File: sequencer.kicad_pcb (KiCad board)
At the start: 2 copper layers, 171.4 x 106.7 mm, 435 parts, among them J1 PJ301CM, J10 PJ301BM, J11 PJ301BM, J12 PJ301BM, J13 PJ301BM, J14 PJ301BM, J15 PJ301BM, J16 PJ301BM, J17 PJ301BM, J18 PJ301BM, J19 PJ301BM, J2 PJ301CM, J20 PJ301BM, J21 PJ301BM, J22 PJ301BM, J23 PJ301BM, J24 PJ301BM, J25 PJ301BM, J26 PJ301BM, J3 PJ301BM, J4 PJ301BM, J5 PJ301BM, J6 PJ301BM, J7 PJ301BM, J8 PJ301BM, J9 PJ301BM, Q1 MMBT3904, Q2 MMBT3904, Q3 MMBT3904, Q4 MMBT3904, Q5 MMBT3904, SW1 TL1105, SW10 TL1105, SW11 TL1105, SW12 TL1105, SW13 TL1105, SW14 TL1105, SW15 TL1105, SW16 TL1105, SW17 TL1105, SW18 TL1105, SW19 EVQQ2, SW2 TL1105, SW20 TL1105, SW21 TL1105, SW22 TL1105, SW23 TL1105, SW24 TL1105, SW25 TL1105, SW26 TL1105, SW27 TL1105, SW28 TL1105, SW29 TL1105, SW3 TL1105, SW30 TL1105, SW31 TL1105, SW32 TL1105, SW33 TL1105, SW34 TL1105, SW35 TL1105, SW36 TL1105, SW37 TL1105, SW38 TL1105, SW39 TL1105, SW4 TL1105, SW5 TL1105, SW6 TL1105, SW7 TL1105, SW8 EVQQ2, SW9 TL1105, U1 VO0600T, U10 LM1117-3.3, U11 74HC165, U12 74HC595, U13 74HC595, U14 74HC595, U15 OPA4172, U16 R-78E5.0-1.0, U2 74LV1T34, U3 STMPS2151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

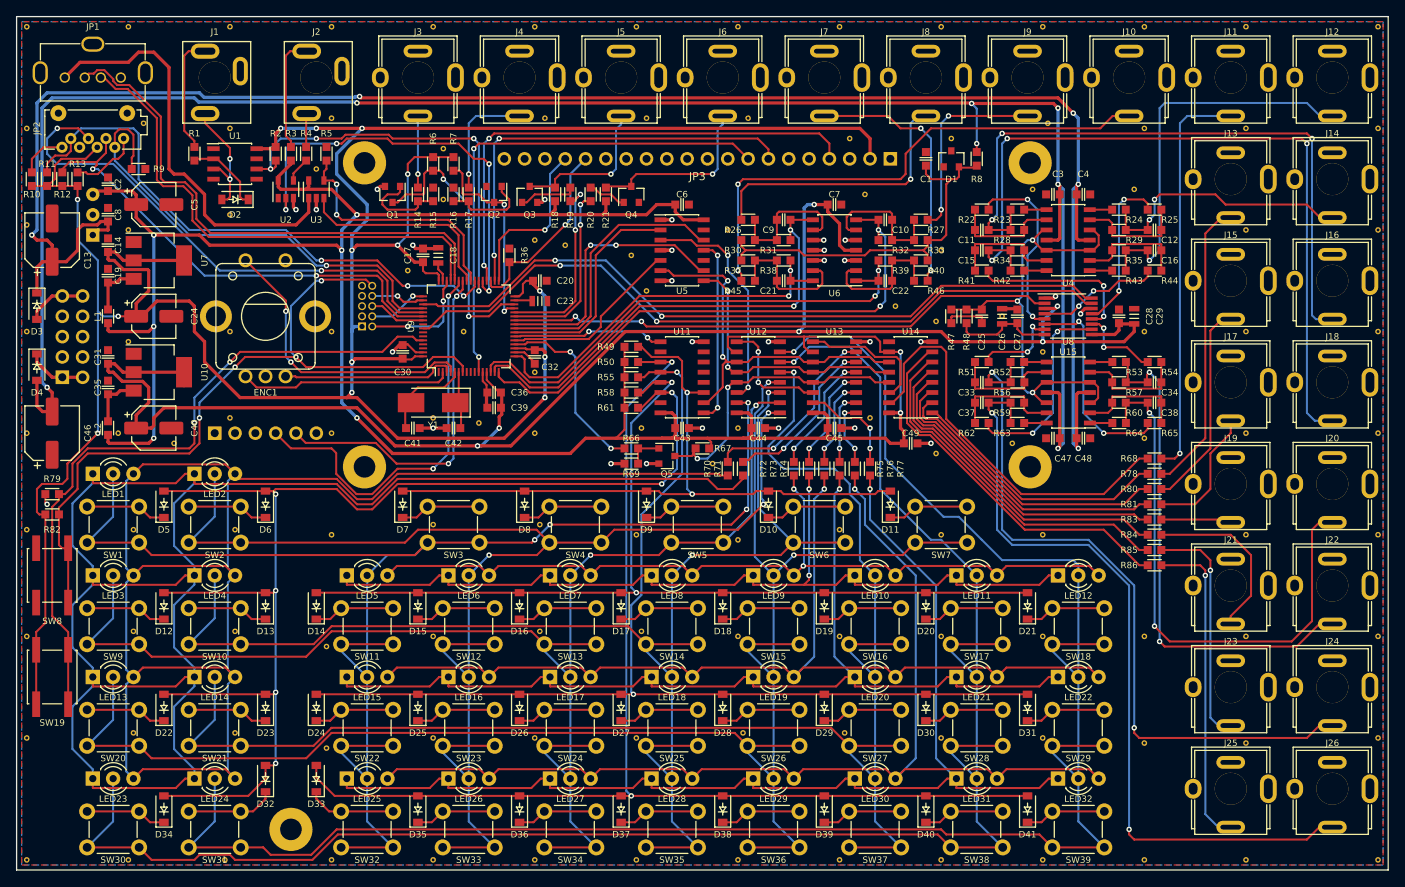
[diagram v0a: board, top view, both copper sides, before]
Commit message: replaced jacks with thonkiconns, updated pcb routing
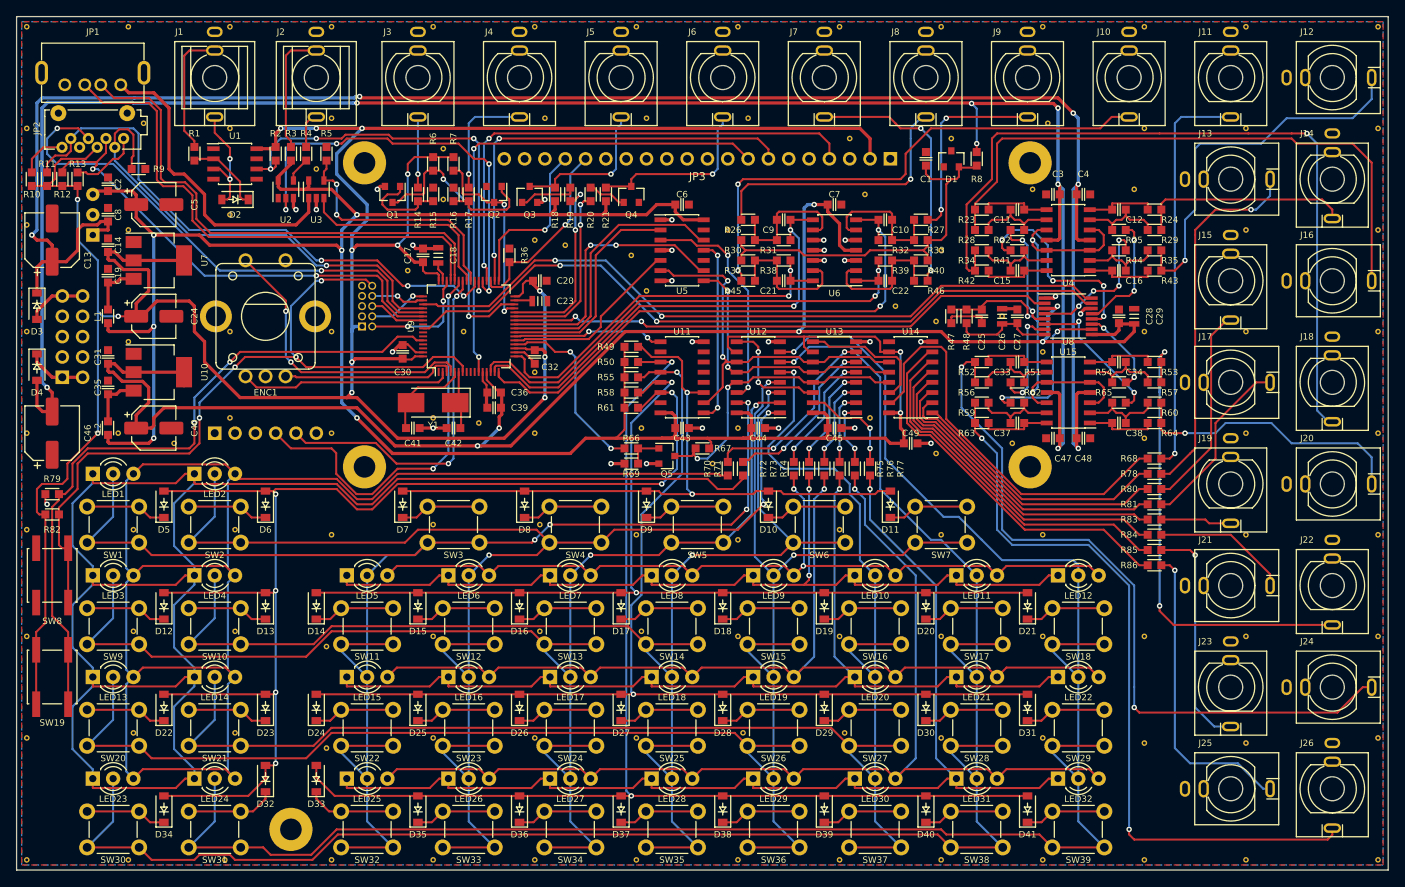
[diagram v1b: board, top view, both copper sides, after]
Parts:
- J1, J2: footprint w_connector:PJ301CM_OFFSET -> w_connector:PJ366ST_Compact
- J10, J11, J12, J13, J14, J15, J16, J17, J18, J19, J20, J21, J22, J23, J24, J25, J26, J3, J4, J5, J6, J7, J8, J9: value PJ301BM -> PJ301M-12_Compact; footprint w_connector:PJ301BM -> w_connector:PJ301M-12_Compact
- JP1: footprint w_connector:MOLEX_USB_105057 -> w_connector:Kycon_USB_KUSBVLPX-AS1N
- moved C37 5.12 mm to (201.9, 88.9)
- moved C38 5.12 mm to (214.6, 88.9)
- moved R62 5.12 mm to (201.9, 86.4), turned to 180 degrees
- moved R65 5.12 mm to (214.6, 86.4), turned to 0 degrees
- moved C11 5.12 mm to (201.9, 62.2)
- moved C12 5.12 mm to (214.6, 62.2)
- moved R22 5.12 mm to (201.9, 64.8), turned to 180 degrees
- moved R25 5.12 mm to (214.6, 64.8), turned to 0 degrees
- moved C15 5.12 mm to (201.9, 69.8)
- moved C16 5.12 mm to (214.6, 69.8)
- moved C33 5.12 mm to (201.9, 81.3)
- moved C34 5.12 mm to (214.6, 81.3)
- moved R41 5.12 mm to (201.9, 67.3), turned to 180 degrees
- moved R44 5.12 mm to (214.6, 67.3), turned to 0 degrees
- moved R51 5.12 mm to (201.9, 83.8), turned to 180 degrees
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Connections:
- C11 pad 1: CV3 -> Net-(C11-Pad1)
- C12 pad 1: CV2 -> Net-(C12-Pad1)
- C15 pad 1: CV4 -> Net-(C15-Pad1)
- C16 pad 1: CV1 -> Net-(C16-Pad1)
- C33 pad 1: CV7 -> Net-(C33-Pad1)
- C34 pad 1: CV6 -> Net-(C34-Pad1)
- C37 pad 1: CV8 -> Net-(C37-Pad1)
- C38 pad 1: CV5 -> Net-(C38-Pad1)
- R23 pad 2: Net-(R23-Pad2) -> Net-(C11-Pad1)
- R24 pad 2: Net-(R24-Pad2) -> Net-(C12-Pad1)
- R42 pad 2: Net-(R42-Pad2) -> Net-(C15-Pad1)
- R43 pad 2: Net-(R43-Pad2) -> Net-(C16-Pad1)
- R52 pad 2: Net-(R52-Pad2) -> Net-(C33-Pad1)
- R53 pad 2: Net-(R53-Pad2) -> Net-(C34-Pad1)
- R63 pad 2: Net-(R63-Pad2) -> Net-(C37-Pad1)
- R64 pad 2: Net-(R64-Pad2) -> Net-(C38-Pad1)
- U15 pad 1: Net-(R64-Pad2) -> Net-(C38-Pad1)
- U15 pad 14: Net-(R63-Pad2) -> Net-(C37-Pad1)
- U15 pad 7: Net-(R53-Pad2) -> Net-(C34-Pad1)
- U15 pad 8: Net-(R52-Pad2) -> Net-(C33-Pad1)
- U4 pad 1: Net-(R43-Pad2) -> Net-(C16-Pad1)
- U4 pad 14: Net-(R42-Pad2) -> Net-(C15-Pad1)
- U4 pad 7: Net-(R24-Pad2) -> Net-(C12-Pad1)
- U4 pad 8: Net-(R23-Pad2) -> Net-(C11-Pad1)
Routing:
- net CV5: track 70.5 -> 35.5 mm, vias 2 -> 1
- net USB_5V: track 52.1 -> 39.1 mm
- net DAC3: track 23.4 -> 14.3 mm
- net CV3: track 83.9 -> 75.0 mm, vias 3 -> 0
- net Net-(C33-Pad1): track 0.00 -> 8.79 mm
- net Net-(C37-Pad1): track 0.00 -> 8.79 mm
- net Net-(C16-Pad1): track 0.00 -> 8.77 mm
- net Net-(C15-Pad1): track 0.00 -> 8.77 mm
- net Net-(C12-Pad1): track 0.00 -> 8.77 mm
- net Net-(C11-Pad1): track 0.00 -> 8.77 mm
- net Net-(C34-Pad1): track 0.00 -> 8.75 mm
- net Net-(C38-Pad1): track 0.00 -> 8.75 mm
- net Net-(J13-Pad3): track 37.6 -> 46.1 mm, vias 0 -> 1
- net DAC5: track 26.2 -> 18.3 mm
- net CV2: track 33.1 -> 26.5 mm, vias 2 -> 0
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
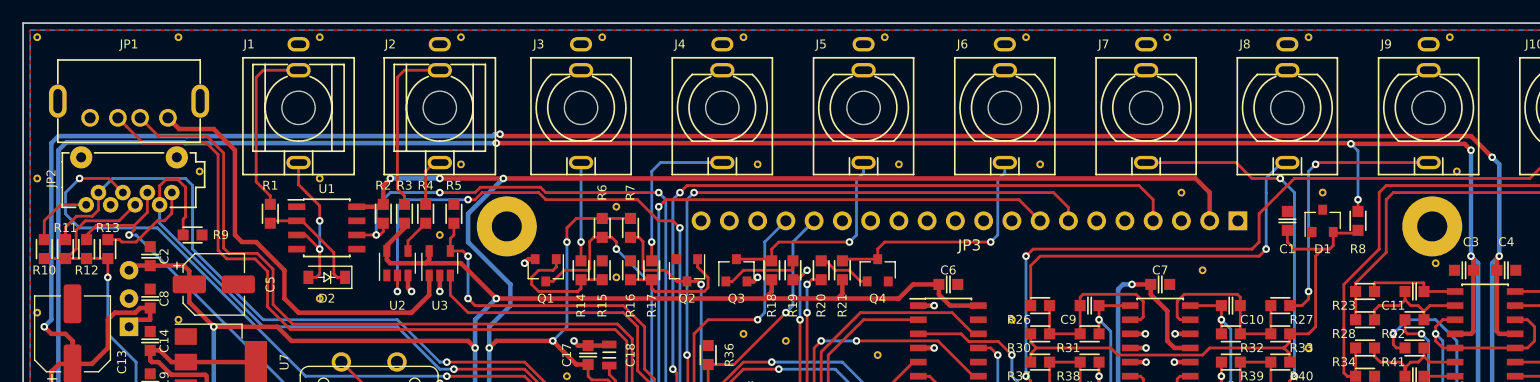
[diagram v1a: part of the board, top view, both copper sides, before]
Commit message: moved usb connector up
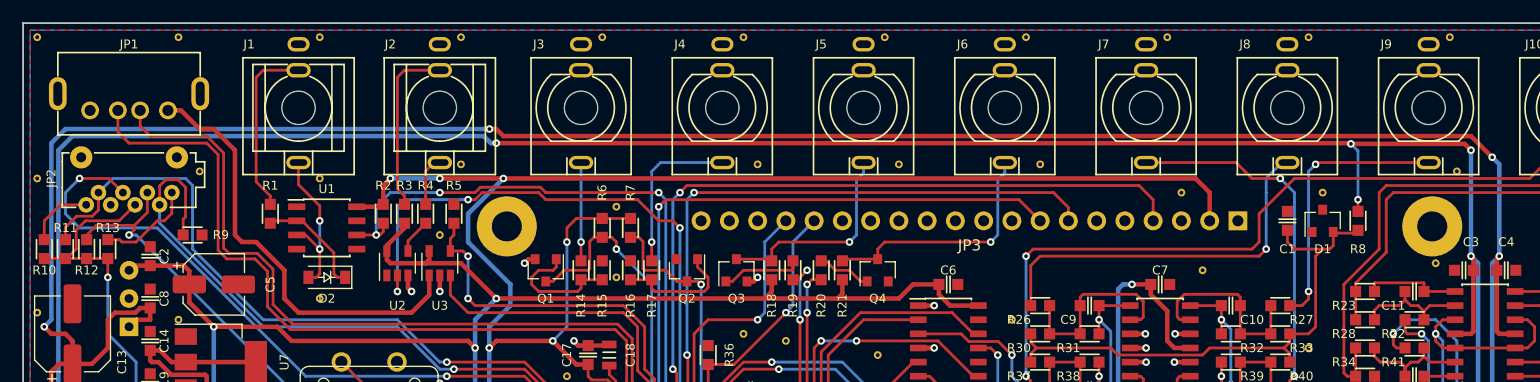
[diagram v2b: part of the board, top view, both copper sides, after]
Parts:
- moved JP1 0.67 mm to (86.4, 44.5)
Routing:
- net USB_D+: track 65.4 -> 66.8 mm
- net USB_D-: track 64.0 -> 65.1 mm

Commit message: updated component values and revision
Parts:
- J1, J2: value PJ301CM -> PJ366ST
- J10, J11, J12, J13, J14, J15, J16, J17, J18, J19, J20, J21, J22, J23, J24, J25, J26, J3, J4, J5, J6, J7, J8, J9: value PJ301M-12_Compact -> PJ398SM
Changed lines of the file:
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@@
   )
   (setup
-    (last_trace_width 0.4064)
+    (last_trace_width 0.254)
     (user_trace_width 0.254)
     (user_trace_width 0.4064)
@@
       (effects (font (size 0.8 0.8) (thickness 0.15)))
     )
-    (fp_text value PJ301M-12_Compact (at 0 0 180) (layer F.Fab)
+    (fp_text value PJ398SM (at 0 0 180) (layer F.Fab)
       (effects (font (size 1 1) (thickness 0.15)))
     )
@@
       (effects (font (size 0.8 0.8) (thickness 0.15)))
     )
-    (fp_text value PJ301M-12_Compact (at 0 0 180) (layer F.Fab)
+    (fp_text value PJ398SM (at 0 0 180) (layer F.Fab)
       (effects (font (size 1 1) (thickness 0.15)))
     )
@@
       (effects (font (size 0.8 0.8) (thickness 0.15)))
     )
-    (fp_text value PJ301M-12_Compact (at 0 0 180) (layer F.Fab)
+    (fp_text value PJ398SM (at 0 0 180) (layer F.Fab)
       (effects (font (size 1 1) (thickness 0.15)))
     )
@@
       (effects (font (size 0.8 0.8) (thickness 0.15)))
     )
-    (fp_text value PJ301M-12_Compact (at 0 0 270) (layer F.Fab)
+    (fp_text value PJ398SM (at 0 0 270) (layer F.Fab)
       (effects (font (size 1 1) (thickness 0.15)))
     )
@@
       (effects (font (size 0.8 0.8) (thickness 0.15)))
     )
-    (fp_text value PJ301M-12_Compact (at 0 0 180) (layer F.Fab)
+    (fp_text value PJ398SM (at 0 0 180) (layer F.Fab)
       (effects (font (size 1 1) (thickness 0.15)))
     )
@@
       (effects (font (size 0.8 0.8) (thickness 0.15)))
     )
-    (fp_text value PJ301M-12_Compact (at 0 0 270) (layer F.Fab)
+    (fp_text value PJ398SM (at 0 0 270) (layer F.Fab)
       (effects (font (size 1 1) (thickness 0.15)))
     )
@@
       (effects (font (size 0.8 0.8) (thickness 0.15)))
     )
-    (fp_text value PJ301M-12_Compact (at 0 0 180) (layer F.Fab)
+    (fp_text value PJ398SM (at 0 0 180) (layer F.Fab)
       (effects (font (size 1 1) (thickness 0.15)))
     )
@@
       (effects (font (size 0.8 0.8) (thickness 0.15)))
     )
-    (fp_text value PJ301M-12_Compact (at 0 0 270) (layer F.Fab)
+    (fp_text value PJ398SM (at 0 0 270) (layer F.Fab)
       (effects (font (size 1 1) (thickness 0.15)))
     )
@@
       (effects (font (size 0.8 0.8) (thickness 0.15)))
     )
-    (fp_text value PJ301M-12_Compact (at 0 0 180) (layer F.Fab)
+    (fp_text value PJ398SM (at 0 0 180) (layer F.Fab)
       (effects (font (size 1 1) (thickness 0.15)))
     )
@@
       (effects (font (size 0.8 0.8) (thickness 0.15)))
     )
-    (fp_text value PJ301M-12_Compact (at 0 0 270) (layer F.Fab)
+    (fp_text value PJ398SM (at 0 0 270) (layer F.Fab)
       (effects (font (size 1 1) (thickness 0.15)))
     )
@@
       (effects (font (size 0.8 0.8) (thickness 0.15)))
     )
-    (fp_text value PJ301M-12_Compact (at 0 0 180) (layer F.Fab)
+    (fp_text value PJ398SM (at 0 0 180) (layer F.Fab)
       (effects (font (size 1 1) (thickness 0.15)))
     )
@@
       (effects (font (size 0.8 0.8) (thickness 0.15)))
     )
-    (fp_text value PJ301M-12_Compact (at 0 0 180) (layer F.Fab)
+    (fp_text value PJ398SM (at 0 0 180) (layer F.Fab)
       (effects (font (size 1 1) (thickness 0.15)))
     )
@@
       (effects (font (size 0.8 0.8) (thickness 0.15)))
     )
-    (fp_text value PJ301M-12_Compact (at 0 0 180) (layer F.Fab)
+    (fp_text value PJ398SM (at 0 0 180) (layer F.Fab)
       (effects (font (size 1 1) (thickness 0.15)))
     )
@@
       (effects (font (size 0.8 0.8) (thickness 0.15)))
     )
-    (fp_text value PJ301M-12_Compact (at 0 0 180) (layer F.Fab)
+    (fp_text value PJ398SM (at 0 0 180) (layer F.Fab)
       (effects (font (size 1 1) (thickness 0.15)))
     )
@@
       (effects (font (size 0.8 0.8) (thickness 0.15)))
     )
-    (fp_text value PJ301M-12_Compact (at 0 0 180) (layer F.Fab)
+    (fp_text value PJ398SM (at 0 0 180) (layer F.Fab)
       (effects (font (size 1 1) (thickness 0.15)))
     )
@@
       (effects (font (size 0.8 0.8) (thickness 0.15)))
     )
-    (fp_text value PJ301M-12_Compact (at 0 0 270) (layer F.Fab)
+    (fp_text value PJ398SM (at 0 0 270) (layer F.Fab)
       (effects (font (size 1 1) (thickness 0.15)))
     )
@@
       (effects (font (size 0.8 0.8) (thickness 0.15)))
     )
-    (fp_text value PJ301M-12_Compact (at 0 0 180) (layer F.Fab)
+    (fp_text value PJ398SM (at 0 0 180) (layer F.Fab)
       (effects (font (size 1 1) (thickness 0.15)))
     )
@@
       (effects (font (size 0.8 0.8) (thickness 0.15)))
     )
-    (fp_text value PJ301M-12_Compact (at 0 0 270) (layer F.Fab)
+    (fp_text value PJ398SM (at 0 0 270) (layer F.Fab)
       (effects (font (size 1 1) (thickness 0.15)))
     )
@@
       (effects (font (size 0.8 0.8) (thickness 0.15)))
     )
-    (fp_text value PJ301M-12_Compact (at 0 0 180) (layer F.Fab)
+    (fp_text value PJ398SM (at 0 0 180) (layer F.Fab)
       (effects (font (size 1 1) (thickness 0.15)))
     )
@@
       (effects (font (size 0.8 0.8) (thickness 0.15)))
     )
-    (fp_text value PJ301M-12_Compact (at 0 0 270) (layer F.Fab)
+    (fp_text value PJ398SM (at 0 0 270) (layer F.Fab)
       (effects (font (size 1 1) (thickness 0.15)))
     )
@@
       (effects (font (size 0.8 0.8) (thickness 0.15)))
     )
-    (fp_text value PJ301M-12_Compact (at 0 0 180) (layer F.Fab)
+    (fp_text value PJ398SM (at 0 0 180) (layer F.Fab)
       (effects (font (size 1 1) (thickness 0.15)))
     )
@@
       (effects (font (size 0.8 0.8) (thickness 0.15)))
     )
-    (fp_text value PJ301M-12_Compact (at 0 0 270) (layer F.Fab)
+    (fp_text value PJ398SM (at 0 0 270) (layer F.Fab)
       (effects (font (size 1 1) (thickness 0.15)))
     )
@@
       (effects (font (size 0.8 0.8) (thickness 0.15)))
     )
-    (fp_text value PJ301M-12_Compact (at 0 0 180) (layer F.Fab)
+    (fp_text value PJ398SM (at 0 0 180) (layer F.Fab)
       (effects (font (size 1 1) (thickness 0.15)))
     )
@@
       (effects (font (size 0.8 0.8) (thickness 0.15)))
     )
-    (fp_text value PJ301M-12_Compact (at 0 0 180) (layer F.Fab)
+    (fp_text value PJ398SM (at 0 0 180) (layer F.Fab)
       (effects (font (size 1 1) (thickness 0.15)))
     )
@@
       (effects (font (size 0.8 0.8) (thickness 0.15)))
     )
-    (fp_text value PJ301CM (at 0 0 180) (layer F.Fab)
+    (fp_text value PJ366ST (at 0 0 180) (layer F.Fab)
       (effects (font (size 1 1) (thickness 0.15)))
     )
@@
       (effects (font (size 0.8 0.8) (thickness 0.15)))
     )
-    (fp_text value PJ301CM (at 0 0 180) (layer F.Fab)
-      (effects (font (size 1 1) (thickness 0.15)))
-    )
+    (fp_text value PJ366ST (at 0 0 180) (layer F.Fab)
+      (effects (font (size 1 1) (thickness 0.15)))
+    )
